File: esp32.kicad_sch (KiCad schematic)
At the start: 9 parts, among them J12 DAT0, J13 DAT_DSP, J14 + -, U10 TXS0108EPW_MODULE, U11 TXS0108EPW_MODULE, U12 TXS0108EPW_MODULE, U9 DOIT_ESP32_DevKit_v1

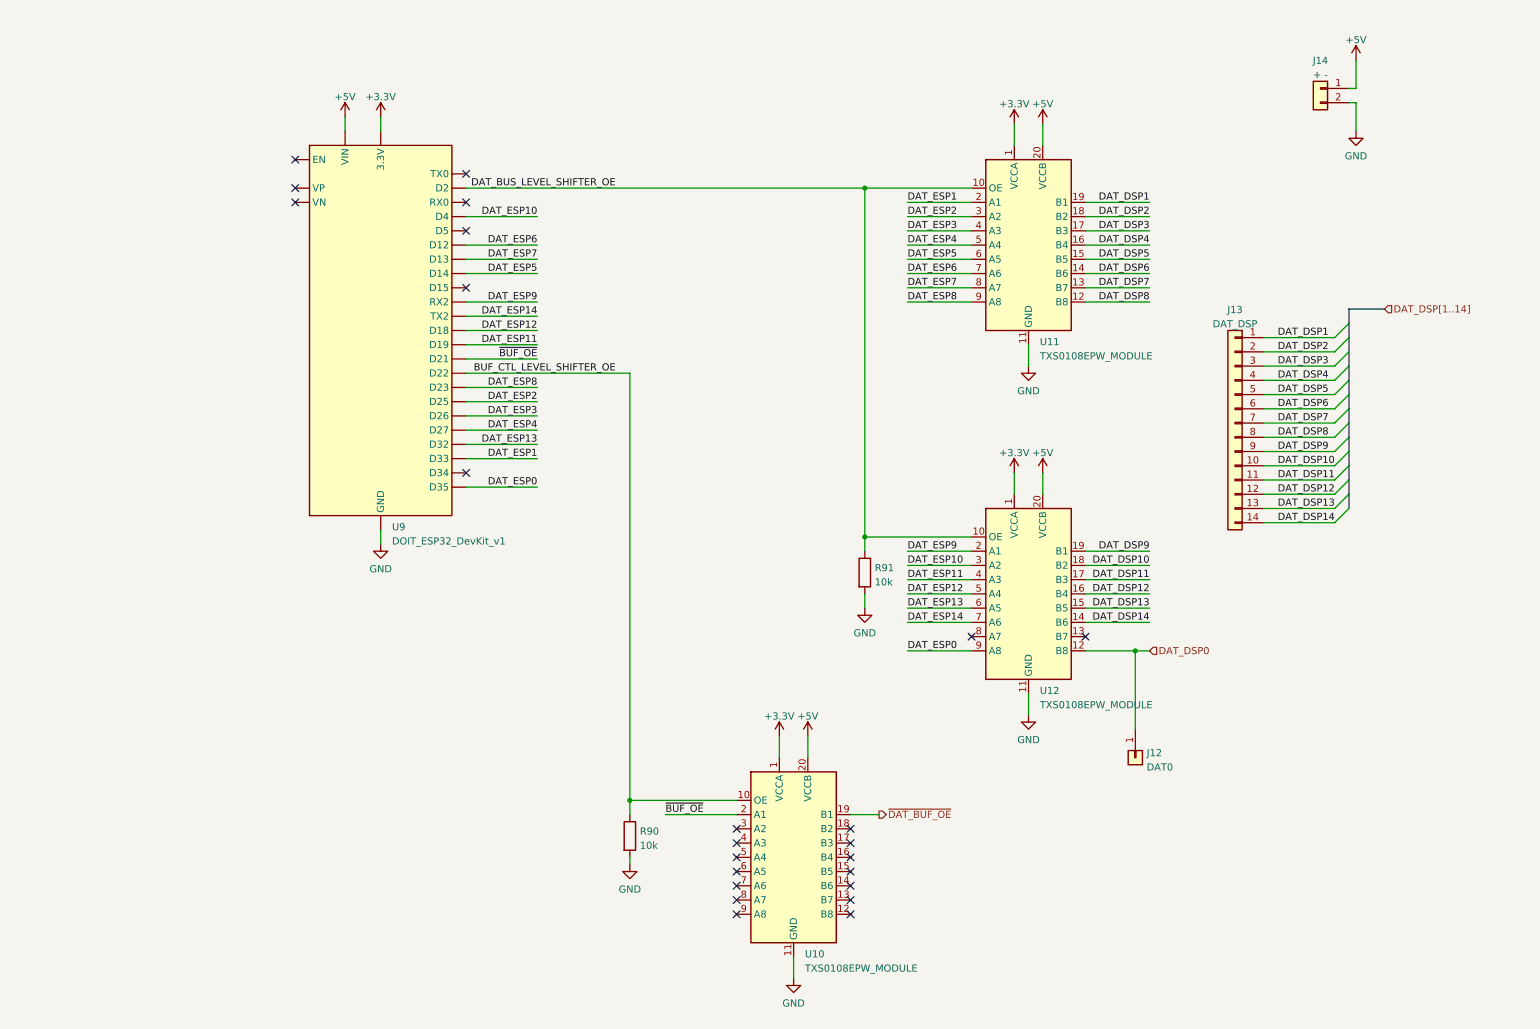
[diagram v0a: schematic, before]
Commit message: Redesigned Level Shifting Schematic
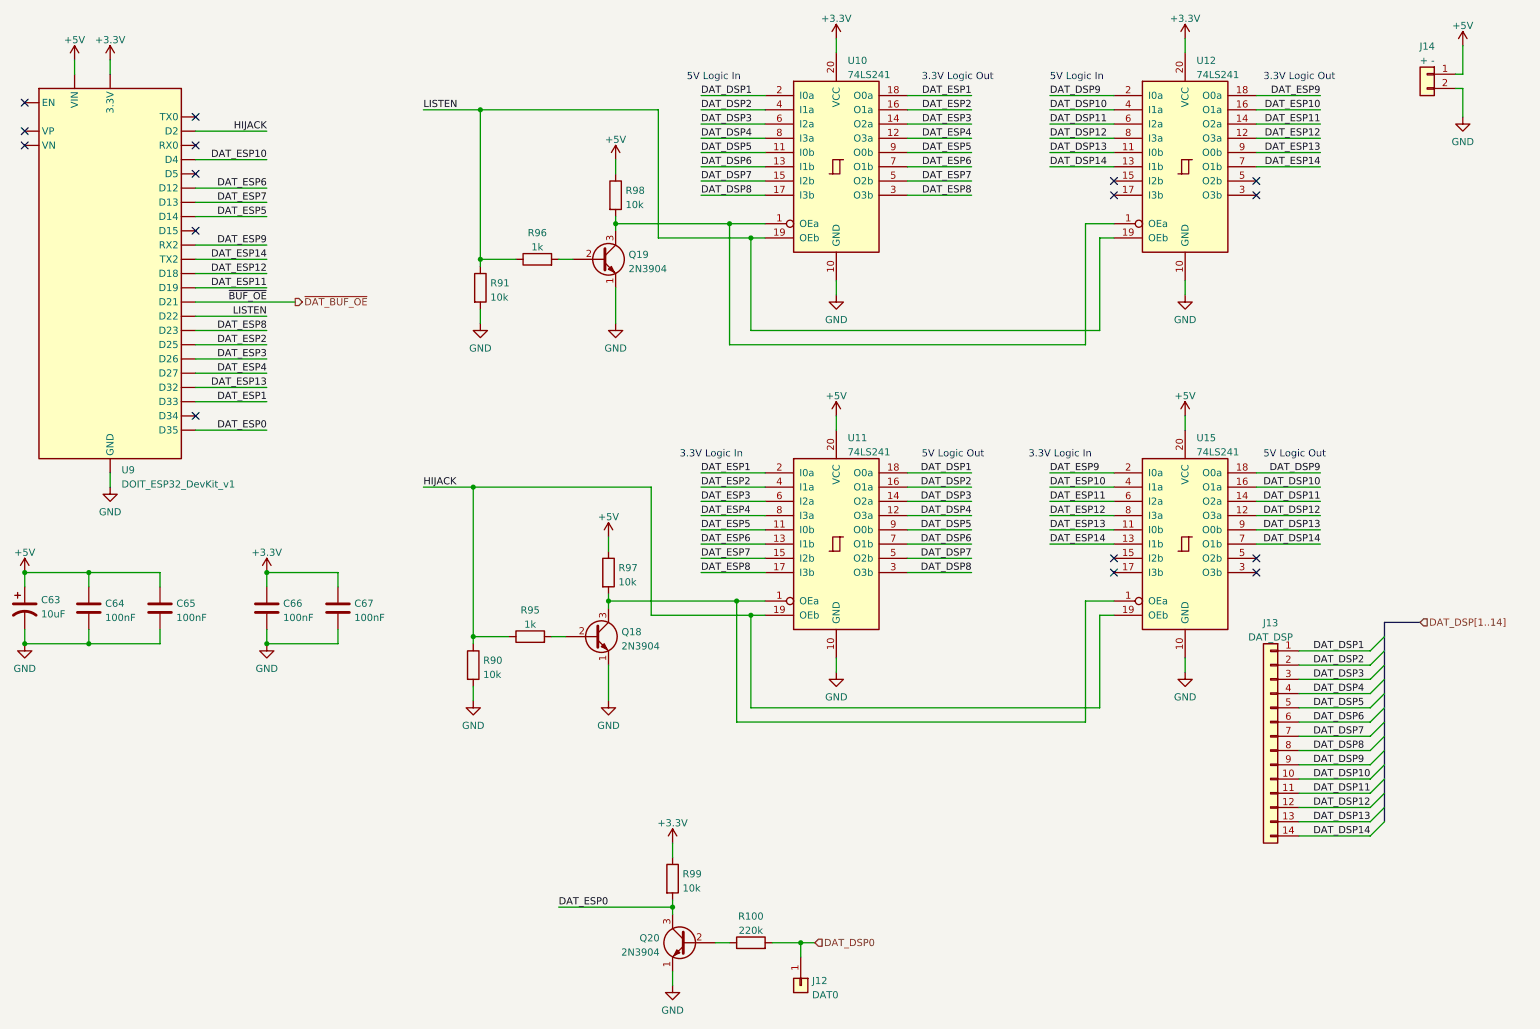
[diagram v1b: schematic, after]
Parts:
- removed U10, U11, U12: TXS0108EPW_MODULE, videonics processor plus - Copy:DIP-20_500_ELL, symbol Videonics Proceessor Plus:TXS0108EPW_MODULE
- added C63: 10uF, symbol Device:C_Polarized_US
- added C64, C65, C66, C67: 100nF, symbol Device:C
- added Q18, Q19: 2N3904, Package_TO_SOT_THT:TO-92_Inline_Wide, symbol Transistor_BJT:2N3904
- added Q20: 2N3904, Package_TO_SOT_THT:TO-92_Inline, symbol Transistor_BJT:2N3904
- added R100: 220k, symbol Device:R
- added R95, R96: 1k, Resistor_THT:R_Axial_DIN0207_L6.3mm_D2.5mm_P10.16mm_Horizontal, symbol Device:R
- added R97, R98: 10k, Resistor_THT:R_Axial_DIN0207_L6.3mm_D2.5mm_P10.16mm_Horizontal, symbol Device:R
- added R99: 10k, symbol Device:R
- added U10, U11, U12, U15: 74LS241, symbol 74xx:74LS241
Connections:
- net ~{BUF_OE} is gone; now on net ~{DAT_BUF_OE}: U9.26 (D21)
- net +3.3V: now also C66.1, C67.1, R99.1, U10.20 (VCC), U12.20 (VCC)
- net +5V: now also C63.1, C64.1, C65.1, R97.1, R98.1, U11.20 (VCC), U15.20 (VCC)
- net DAT_DSP0: now also R100.2
- net DAT_DSP1: now also U10.2 (I0a), U11.18 (O0a)
- net DAT_DSP10: now also U12.4 (I1a), U15.16 (O1a)
- net DAT_DSP11: now also U12.6 (I2a), U15.14 (O2a)
- net DAT_DSP12: now also U12.8 (I3a), U15.12 (O3a)
- net DAT_DSP13: now also U12.11 (I0b), U15.9 (O0b)
- net DAT_DSP14: now also U12.13 (I1b), U15.7 (O1b)
- net DAT_DSP2: now also U10.4 (I1a), U11.16 (O1a)
- net DAT_DSP3: now also U10.6 (I2a), U11.14 (O2a)
- net DAT_DSP4: now also U10.8 (I3a), U11.12 (O3a)
- net DAT_DSP5: now also U10.11 (I0b), U11.9 (O0b)
- net DAT_DSP6: now also U10.13 (I1b), U11.7 (O1b)
- net DAT_DSP7: now also U10.15 (I2b), U11.5 (O2b)
- net DAT_DSP8: now also U10.17 (I3b), U11.3 (O3b)
- net DAT_DSP9: now also U12.2 (I0a), U15.18 (O0a)
- net DAT_ESP0: now also Q20.3 (C), R99.2
- net DAT_ESP1: now also U10.18 (O0a), U11.2 (I0a)
- net DAT_ESP10: now also U12.16 (O1a), U15.4 (I1a)
- net DAT_ESP11: now also U12.14 (O2a), U15.6 (I2a)
- net DAT_ESP12: now also U12.12 (O3a), U15.8 (I3a)
- net DAT_ESP13: now also U12.9 (O0b), U15.11 (I0b)
- net DAT_ESP14: now also U12.7 (O1b), U15.13 (I1b)
- net DAT_ESP2: now also U10.16 (O1a), U11.4 (I1a)
- net DAT_ESP3: now also U10.14 (O2a), U11.6 (I2a)
- net DAT_ESP4: now also U10.12 (O3a), U11.8 (I3a)
- net DAT_ESP5: now also U10.9 (O0b), U11.11 (I0b)
- net DAT_ESP6: now also U10.7 (O1b), U11.13 (I1b)
- net DAT_ESP7: now also U10.5 (O2b), U11.15 (I2b)
- net DAT_ESP8: now also U10.3 (O3b), U11.17 (I3b)
- net DAT_ESP9: now also U12.18 (O0a), U15.2 (I0a)
- net GND: now also C63.2, C64.2, C65.2, C66.2, C67.2, Q18.1 (E), Q19.1 (E), Q20.1 (E), U10.10 (GND), U11.10 (GND), U12.10 (GND), U15.10 (GND)
- net BUF_CTL_LEVEL_SHIFTER_OE renamed HIJACK
- net HIJACK: now also U9.19 (D2), R95.1, U11.19 (OEb), U15.19 (OEb); no longer U9.29 (D22)
- net DAT_BUS_LEVEL_SHIFTER_OE renamed LISTEN
- net LISTEN: now also U9.29 (D22), R96.1, U10.19 (OEb), U12.19 (OEb); no longer U9.19 (D2)
- new net: Q19.2 (B), R96.2
- new net: Q19.3 (C), R98.2, U10.1 (OEa), U12.1 (OEa)
- new net: Q18.3 (C), R97.2, U11.1 (OEa), U15.1 (OEa)
- new net: Q18.2 (B), R95.2
- new net: Q20.2 (B), R100.1
- no-connect marks 24 -> 16
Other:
- note added: "3.3V Logic In"
- note added: "3.3V Logic Out"
- note added: "5V Logic In"
- note added: "5V Logic Out"
- moved on the sheet: J12, J13, J14, U9

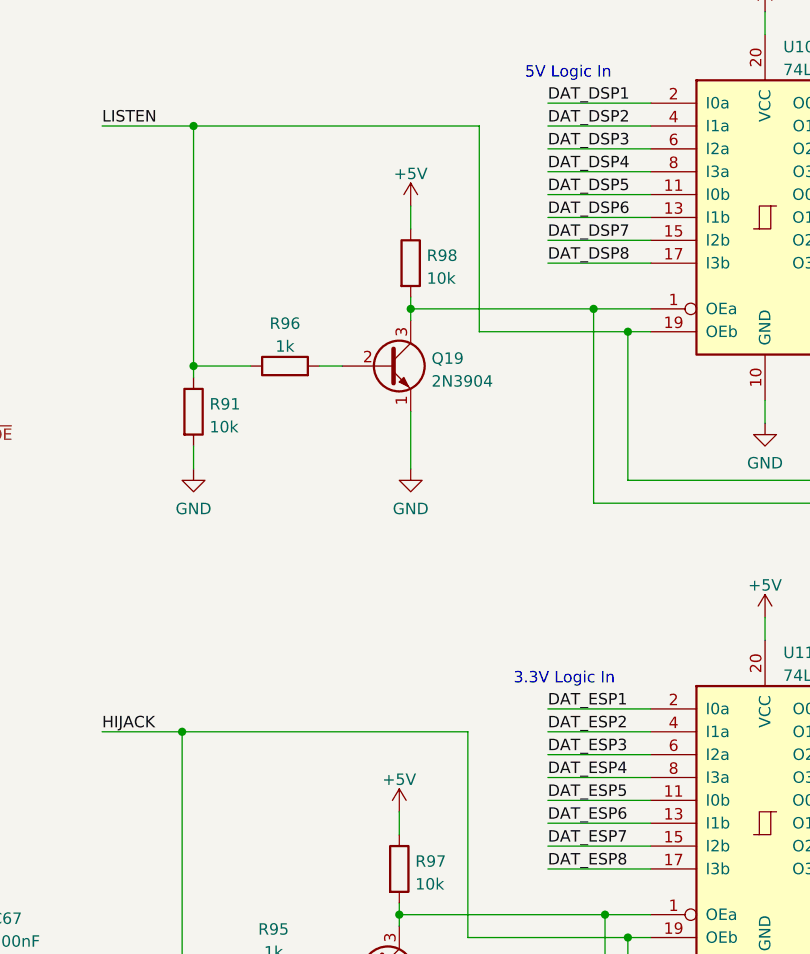
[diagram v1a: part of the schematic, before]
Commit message: Changed level shifter inverter supply from 5V to 3.3V
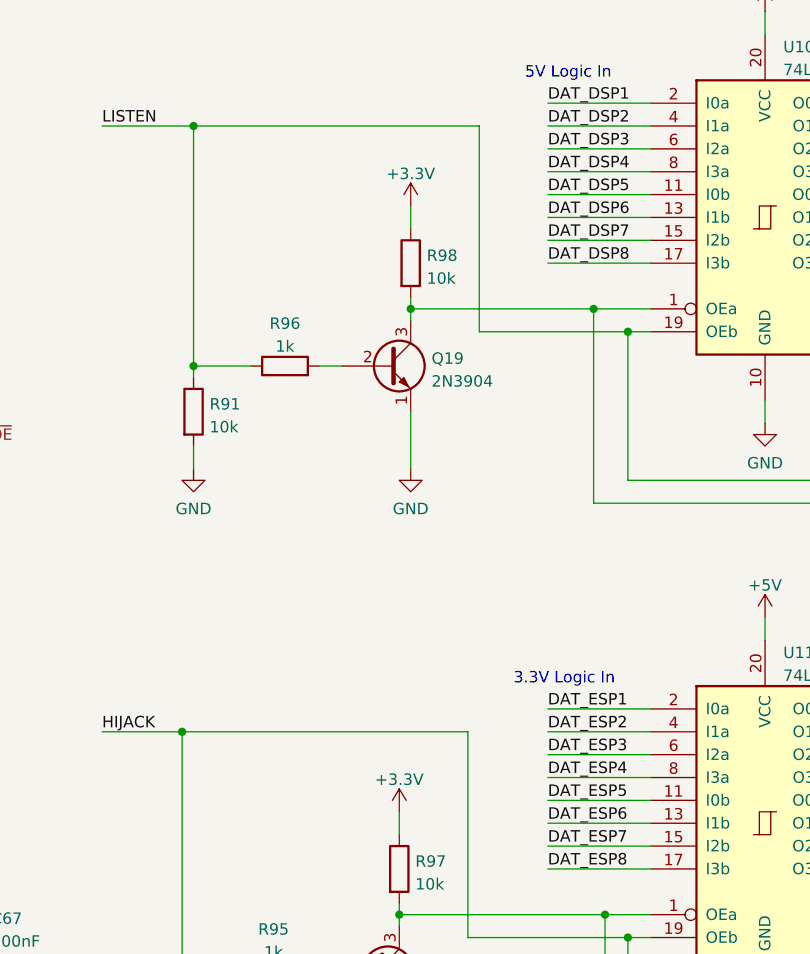
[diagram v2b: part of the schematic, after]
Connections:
- net +3.3V: now also R97.1, R98.1
- net +5V: no longer R97.1, R98.1
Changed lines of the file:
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@@
-    (pin "1")
-  )
-  (symbol (lib_id "power:+5V") (at 124.46 107.95 0) (unit 1)
-    (in_bom yes) (on_board yes) (fields_autoplaced)
-    (property "Reference" "#PWR09" (id 0) (at 124.46 111.76 0)
-      (effects (font (size 1.27 1.27)) hide)
-    )
-    (property "Value" "+5V" (id 1) (at 124.46 104.3742 0))
-    (property "Footprint" "" (id 2) (at 124.46 107.95 0)
-      (effects (font (size 1.27 1.27)) hide)
-    )
-    (property "Datasheet" "" (id 3) (at 124.46 107.95 0)
-      (effects (font (size 1.27 1.27)) hide)
-    )
     (pin "1")
   )
@@
     (pin "2")
   )
+  (symbol (lib_id "power:+3.3V") (at 125.73 40.64 0) (unit 1)
+    (in_bom yes) (on_board yes) (fields_autoplaced)
+    (property "Reference" "#PWR?" (id 0) (at 125.73 44.45 0)
+      (effects (font (size 1.27 1.27)) hide)
+    )
+    (property "Value" "+3.3V" (id 1) (at 125.73 37.0642 0))
+    (property "Footprint" "" (id 2) (at 125.73 40.64 0)
+      (effects (font (size 1.27 1.27)) hide)
+    )
+    (property "Datasheet" "" (id 3) (at 125.73 40.64 0)
+      (effects (font (size 1.27 1.27)) hide)
+    )
+    (pin "1")
+  )
   (symbol (lib_id "Connector_Generic:Conn_01x01") (at 158.75 187.96 270) (unit 1)
     (in_bom yes) (on_board yes) (fields_autoplaced)
@@
     (pin "8")
     (pin "9")
+  )
+  (symbol (lib_id "power:+3.3V") (at 124.46 107.95 0) (unit 1)
+    (in_bom yes) (on_board yes) (fields_autoplaced)
+    (property "Reference" "#PWR?" (id 0) (at 124.46 111.76 0)
+      (effects (font (size 1.27 1.27)) hide)
+    )
+    (property "Value" "+3.3V" (id 1) (at 124.46 104.3742 0))
+    (property "Footprint" "" (id 2) (at 124.46 107.95 0)
+      (effects (font (size 1.27 1.27)) hide)
+    )
+    (property "Datasheet" "" (id 3) (at 124.46 107.95 0)
+      (effects (font (size 1.27 1.27)) hide)
+    )
+    (pin "1")
   )
   (symbol (lib_id "power:GND") (at 227.33 132.08 0) (unit 1)
@@
     (pin "9")
   )
-  (symbol (lib_id "power:+5V") (at 125.73 40.64 0) (unit 1)
-    (in_bom yes) (on_board yes) (fields_autoplaced)
-    (property "Reference" "#PWR011" (id 0) (at 125.73 44.45 0)
-      (effects (font (size 1.27 1.27)) hide)
-    )
-    (property "Value" "+5V" (id 1) (at 125.73 37.0642 0))
-    (property "Footprint" "" (id 2) (at 125.73 40.64 0)
-      (effects (font (size 1.27 1.27)) hide)
-    )
-    (property "Datasheet" "" (id 3) (at 125.73 40.64 0)
-      (effects (font (size 1.27 1.27)) hide)
-    )
-    (pin "1")
-  )
   (symbol (lib_id "Device:C") (at 44.45 120.65 0) (unit 1)

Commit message: Minor formatting updates
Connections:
- net +3.3V: now also U12.15 (I2b), U12.17 (I3b), U12.3 (O3b), U12.5 (O2b)
- net +5V: now also U15.15 (I2b), U15.17 (I3b), U15.3 (O3b), U15.5 (O2b)
- net DAT_ESP10: now also U9.23 (D5); no longer U9.20 (D4)
- net DAT_ESP6: now also U9.18 (D15); no longer U9.12 (D12)
- no-connect marks 16 -> 8
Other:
- note added: "Black"
- note added: "Blue"
- note added: "Green"
- note added: "Note! Has changed from D12 to D15"
- note added: "Note! Has changed from D4 to D5"
- note added: "Red"
- note added: "White"
- note added: "Yellow"

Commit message: update footprints
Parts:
- C63, C64, C65, C66, C67: footprint (none) -> Capacitor_THT:C_Disc_D4.7mm_W2.5mm_P5.00mm
- R100, R99: footprint (none) -> Resistor_THT:R_Axial_DIN0207_L6.3mm_D2.5mm_P10.16mm_Horizontal
- U10, U11, U12, U15: footprint (none) -> Package_DIP:DIP-20_W7.62mm
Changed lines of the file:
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@@
       (effects (font (size 1.27 1.27)) (justify left))
     )
-    (property "Footprint" "" (id 2) (at 20.32 120.65 0)
+    (property "Footprint" "Capacitor_THT:C_Disc_D4.7mm_W2.5mm_P5.00mm" (id 2) (at 20.32 120.65 0)
       (effects (font (size 1.27 1.27)) hide)
     )
@@
   (symbol (lib_id "power:+3.3V") (at 242.57 45.72 270) (unit 1)
     (in_bom yes) (on_board yes) (fields_autoplaced)
-    (property "Reference" "#PWR?" (id 0) (at 238.76 45.72 0)
+    (property "Reference" "#PWR0257" (id 0) (at 238.76 45.72 0)
       (effects (font (size 1.27 1.27)) hide)
     )
@@
       (effects (font (size 1.27 1.27)) (justify left))
     )
-    (property "Footprint" "" (id 2) (at 64.4652 124.46 0)
+    (property "Footprint" "Capacitor_THT:C_Disc_D4.7mm_W2.5mm_P5.00mm" (id 2) (at 64.4652 124.46 0)
       (effects (font (size 1.27 1.27)) hide)
     )
@@
       (effects (font (size 1.27 1.27)) (justify left))
     )
-    (property "Footprint" "" (id 2) (at 227.33 109.22 0)
+    (property "Footprint" "Package_DIP:DIP-20_W7.62mm" (id 2) (at 227.33 109.22 0)
       (effects (font (size 1.27 1.27)) hide)
     )
@@
   (symbol (lib_id "power:+3.3V") (at 125.73 40.64 0) (unit 1)
     (in_bom yes) (on_board yes) (fields_autoplaced)
-    (property "Reference" "#PWR?" (id 0) (at 125.73 44.45 0)
+    (property "Reference" "#PWR0254" (id 0) (at 125.73 44.45 0)
       (effects (font (size 1.27 1.27)) hide)
     )
@@
       (effects (font (size 1.27 1.27)) (justify left))
     )
-    (property "Footprint" "" (id 2) (at 227.33 41.91 0)
+    (property "Footprint" "Package_DIP:DIP-20_W7.62mm" (id 2) (at 227.33 41.91 0)
       (effects (font (size 1.27 1.27)) hide)
     )
@@
   (symbol (lib_id "power:+3.3V") (at 124.46 107.95 0) (unit 1)
     (in_bom yes) (on_board yes) (fields_autoplaced)
-    (property "Reference" "#PWR?" (id 0) (at 124.46 111.76 0)
+    (property "Reference" "#PWR0253" (id 0) (at 124.46 111.76 0)
       (effects (font (size 1.27 1.27)) hide)
     )
@@
       (effects (font (size 1.27 1.27)) (justify left))
     )
-    (property "Footprint" "" (id 2) (at 45.4152 124.46 0)
+    (property "Footprint" "Capacitor_THT:C_Disc_D4.7mm_W2.5mm_P5.00mm" (id 2) (at 45.4152 124.46 0)
       (effects (font (size 1.27 1.27)) hide)
     )
@@
   (symbol (lib_id "power:+5V") (at 212.09 113.03 90) (unit 1)
     (in_bom yes) (on_board yes) (fields_autoplaced)
-    (property "Reference" "#PWR?" (id 0) (at 215.9 113.03 0)
+    (property "Reference" "#PWR0255" (id 0) (at 215.9 113.03 0)
       (effects (font (size 1.27 1.27)) hide)
     )
@@
       (effects (font (size 1.27 1.27)) (justify left))
     )
-    (property "Footprint" "" (id 2) (at 165.1 41.91 0)
+    (property "Footprint" "Package_DIP:DIP-20_W7.62mm" (id 2) (at 165.1 41.91 0)
       (effects (font (size 1.27 1.27)) hide)
     )
@@
       (effects (font (size 1.27 1.27)) (justify left))
     )
-    (property "Footprint" "" (id 2) (at 77.1652 124.46 0)
+    (property "Footprint" "Capacitor_THT:C_Disc_D4.7mm_W2.5mm_P5.00mm" (id 2) (at 77.1652 124.46 0)
       (effects (font (size 1.27 1.27)) hide)
     )
@@
       (effects (font (size 1.27 1.27)) (justify left))
     )
-    (property "Footprint" "" (id 2) (at 134.112 168.91 90)
+    (property "Footprint" "Resistor_THT:R_Axial_DIN0207_L6.3mm_D2.5mm_P10.16mm_Horizontal" (id 2) (at 134.112 168.91 90)
       (effects (font (size 1.27 1.27)) hide)
     )
@@
   (symbol (lib_id "power:+5V") (at 242.57 113.03 270) (unit 1)
     (in_bom yes) (on_board yes) (fields_autoplaced)
-    (property "Reference" "#PWR?" (id 0) (at 238.76 113.03 0)
+    (property "Reference" "#PWR0256" (id 0) (at 238.76 113.03 0)
       (effects (font (size 1.27 1.27)) hide)
     )
@@
   (symbol (lib_id "power:+3.3V") (at 212.09 45.72 90) (unit 1)
     (in_bom yes) (on_board yes) (fields_autoplaced)
-    (property "Reference" "#PWR?" (id 0) (at 215.9 45.72 0)
+    (property "Reference" "#PWR0252" (id 0) (at 215.9 45.72 0)
       (effects (font (size 1.27 1.27)) hide)
     )
@@
       (effects (font (size 1.27 1.27)) (justify left))
     )
-    (property "Footprint" "" (id 2) (at 32.7152 124.46 0)
+    (property "Footprint" "Capacitor_THT:C_Disc_D4.7mm_W2.5mm_P5.00mm" (id 2) (at 32.7152 124.46 0)
       (effects (font (size 1.27 1.27)) hide)
     )
@@
       (effects (font (size 1.27 1.27)) (justify left))
     )
-    (property "Footprint" "" (id 2) (at 165.1 109.22 0)
+    (property "Footprint" "Package_DIP:DIP-20_W7.62mm" (id 2) (at 165.1 109.22 0)
       (effects (font (size 1.27 1.27)) hide)
     )
@@
     (property "Reference" "R100" (id 0) (at 149.86 175.6242 90))
     (property "Value" "220k" (id 1) (at 149.86 178.1611 90))
-    (property "Footprint" "" (id 2) (at 149.86 182.118 90)
-      (effects (font (size 1.27 1.27)) hide)
-    )
+    (property "Footprint" "Resistor_THT:R_Axial_DIN0207_L6.3mm_D2.5mm_P10.16mm_Horizontal" (id 2) (at 149.86 182.118 90)
+      (effects (font (size 1.27 1.27)) hide)
+    )
